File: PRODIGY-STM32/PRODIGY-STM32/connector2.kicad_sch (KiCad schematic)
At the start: 1 part, among them J2 DF40C-100DS-0.4V(51)

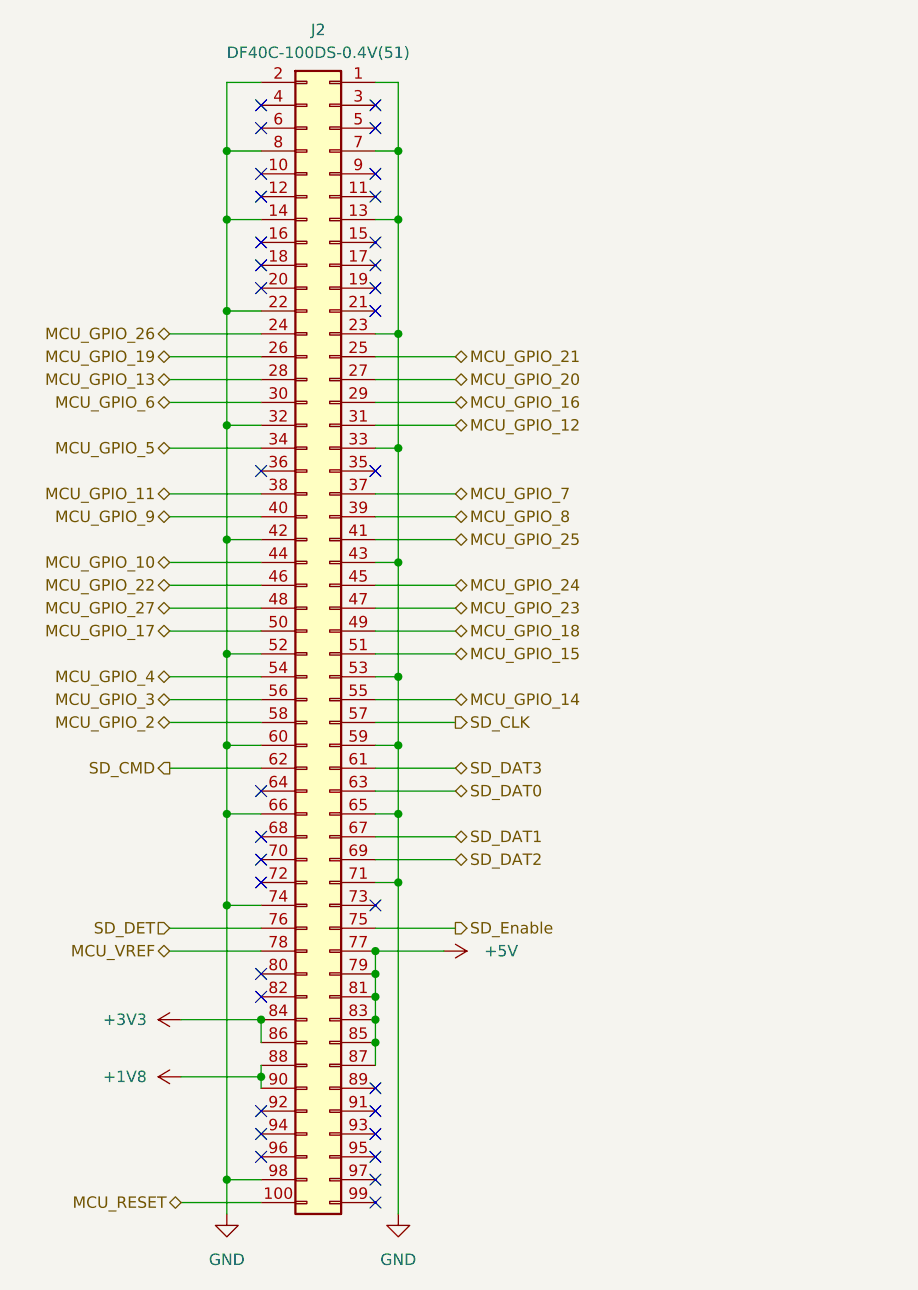
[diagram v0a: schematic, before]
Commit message: stm32 schematic finished
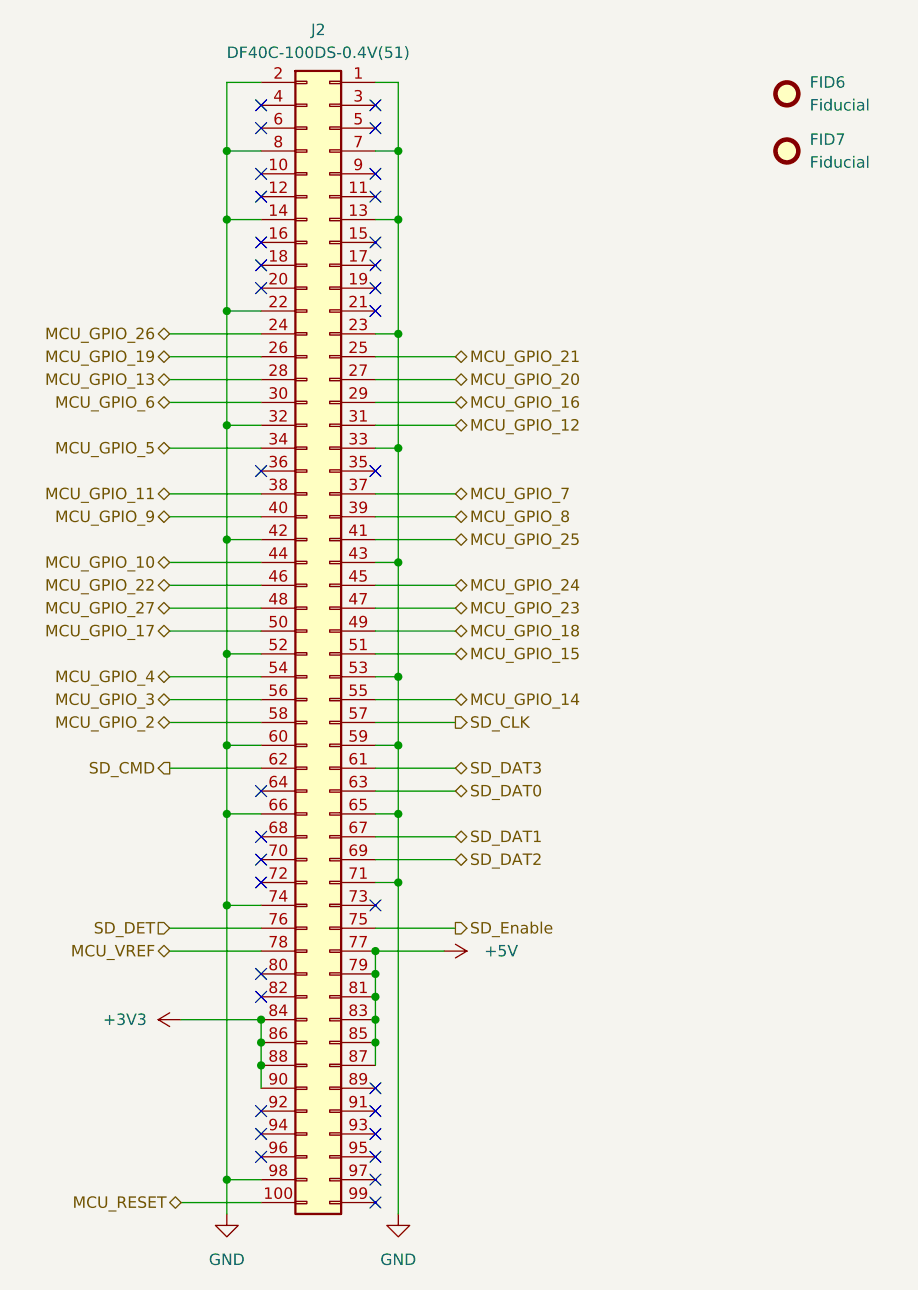
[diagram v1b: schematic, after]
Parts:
- added FID6, FID7: Fiducial, symbol Mechanical:Fiducial
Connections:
- net +1V8 is gone; now on net +3V3: J2.88, J2.90
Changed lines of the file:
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@@
+	)
+	(junction
+		(at 132.08 146.05)
+		(diameter 0)
+		(color 0 0 0 0)
 	)
 	(junction
@@
 	)
 	(junction
+		(at 132.08 143.51)
+		(diameter 0)
+		(color 0 0 0 0)
+	)
+	(junction
 		(at 144.78 143.51)
 		(diameter 0)
@@
 	)
 	(junction
-		(at 132.08 147.32)
-		(diameter 0)
-		(color 0 0 0 0)
-	)
-	(junction
 		(at 128.27 62.23)
 		(diameter 0)
@@
 	(wire
 		(pts
-			(xy 132.08 147.32) (xy 132.08 148.59)
-		)
-		(stroke
-			(width 0)
-			(type default)
-		)
-	)
-	(wire
-		(pts
 			(xy 128.27 44.45) (xy 128.27 52.07)
 		)
@@
 	(wire
 		(pts
-			(xy 132.08 147.32) (xy 132.08 146.05)
-		)
-		(stroke
-			(width 0)
-			(type default)
-		)
-	)
-	(wire
-		(pts
 			(xy 144.78 120.65) (xy 153.67 120.65)
 		)
@@
 	(wire
 		(pts
+			(xy 132.08 143.51) (xy 132.08 146.05)
+		)
+		(stroke
+			(width 0)
+			(type default)
+		)
+	)
+	(wire
+		(pts
 			(xy 147.32 52.07) (xy 147.32 44.45)
 		)
@@
 	(wire
 		(pts
-			(xy 123.19 147.32) (xy 132.08 147.32)
-		)
-		(stroke
-			(width 0)
-			(type default)
-		)
-	)
-	(wire
-		(pts
 			(xy 121.92 95.25) (xy 132.08 95.25)
 		)
@@
 		(pts
 			(xy 121.92 133.35) (xy 132.08 133.35)
+		)
+		(stroke
+			(width 0)
+			(type default)
+		)
+	)
+	(wire
+		(pts
+			(xy 132.08 146.05) (xy 132.08 148.59)
 		)
 		(stroke
@@
 		(on_board yes)
 		(dnp no)
-		(property "Reference" "#PWR023"
+		(property "Reference" "#PWR039"
 			(at 148.59 133.35 0)
 			(effects
@@
 			(project "PRODIGY-STM32"
 				(path "/f2f1c781-b8fe-416b-b7a0-b424640c1d9f/f8ef92a9-2b6b-4a6a-82b5-94550f671624"
-					(reference "#PWR023")
+					(reference "#PWR039")
 					(unit 1)
 				)
@@
 	)
 	(symbol
-		(lib_id "power:+1V8")
-		(at 123.19 147.32 90)
+		(lib_id "Mechanical:Fiducial")
+		(at 190.5 38.1 0)
 		(unit 1)
 		(exclude_from_sim no)
@@
 		(dnp no)
 		(fields_autoplaced yes)
-		(property "Reference" "#PWR020"
-			(at 127 147.32 0)
-			(effects
-				(font
-					(size 1.27 1.27)
-				)
-				(hide yes)
-			)
-		)
-		(property "Value" "+1V8"
-			(at 119.38 147.3199 90)
+		(property "Reference" "FID6"
+			(at 193.04 36.8299 0)
 			(effects
 				(font
@@
 			)
 		)
+		(property "Value" "Fiducial"
+			(at 193.04 39.3699 0)
+			(effects
+				(font
+					(size 1.27 1.27)
+				)
+				(justify left)
+			)
+		)
 		(property "Footprint" ""
-			(at 123.19 147.32 0)
-			(effects
-				(font
-					(size 1.27 1.27)
-				)
-				(hide yes)
-			)
-		)
-		(property "Datasheet" ""
-			(at 123.19 147.32 0)
-			(effects
-				(font
-					(size 1.27 1.27)
-				)
-				(hide yes)
-			)
-		)
-		(property "Description" "Power symbol creates a global label with name \"+1V8\""
-			(at 123.19 147.32 0)
-			(effects
-				(font
-					(size 1.27 1.27)
-				)
-				(hide yes)
-			)
-		)
-		(pin "1"
+			(at 190.5 38.1 0)
+			(effects
+				(font
+					(size 1.27 1.27)
+				)
+				(hide yes)
+			)
+		)
+		(property "Datasheet" "~"
+			(at 190.5 38.1 0)
+			(effects
+				(font
+					(size 1.27 1.27)
+				)
+				(hide yes)
+			)
+		)
+		(property "Description" "Fiducial Marker"
+			(at 190.5 38.1 0)
+			(effects
+				(font
+					(size 1.27 1.27)
+				)
+				(hide yes)
+			)
 		)
 		(instances
 			(project "PRODIGY-STM32"
 				(path "/f2f1c781-b8fe-416b-b7a0-b424640c1d9f/f8ef92a9-2b6b-4a6a-82b5-94550f671624"
-					(reference "#PWR020")
+					(reference "FID6")
+					(unit 1)
+				)
+			)
+		)
+	)
+	(symbol
+		(lib_id "Mechanical:Fiducial")
+		(at 190.5 44.45 0)
+		(unit 1)
+		(exclude_from_sim no)
+		(in_bom yes)
+		(on_board yes)
+		(dnp no)
+		(fields_autoplaced yes)
+		(property "Reference" "FID7"
+			(at 193.04 43.1799 0)
+			(effects
+				(font
+					(size 1.27 1.27)
+				)
+				(justify left)
+			)
+		)
+		(property "Value" "Fiducial"
+			(at 193.04 45.7199 0)
+			(effects
+				(font
+					(size 1.27 1.27)
+				)
+				(justify left)
+			)
+		)
+		(property "Footprint" ""
+			(at 190.5 44.45 0)
+			(effects
+				(font
+					(size 1.27 1.27)
+				)
+				(hide yes)
+			)
+		)
+		(property "Datasheet" "~"
+			(at 190.5 44.45 0)
+			(effects
+				(font
+					(size 1.27 1.27)
+				)
+				(hide yes)
+			)
+		)
+		(property "Description" "Fiducial Marker"
+			(at 190.5 44.45 0)
+			(effects
+				(font
+					(size 1.27 1.27)
+				)
+				(hide yes)
+			)
+		)
+		(instances
+			(project "PRODIGY-STM32"
+				(path "/f2f1c781-b8fe-416b-b7a0-b424640c1d9f/f8ef92a9-2b6b-4a6a-82b5-94550f671624"
+					(reference "FID7")
 					(unit 1)
 				)
@@
 		(dnp no)
 		(fields_autoplaced yes)
-		(property "Reference" "#PWR021"
+		(property "Reference" "#PWR037"
 			(at 128.27 168.91 0)
 			(effects
@@
 			(project "PRODIGY-STM32"
 				(path "/f2f1c781-b8fe-416b-b7a0-b424640c1d9f/f8ef92a9-2b6b-4a6a-82b5-94550f671624"
-					(reference "#PWR021")
+					(reference "#PWR037")
 					(unit 1)
 				)
@@
 		(dnp no)
 		(fields_autoplaced yes)
-		(property "Reference" "#PWR019"
+		(property "Reference" "#PWR035"
 			(at 127 140.97 0)
 			(effects
@@
 			(project "PRODIGY-STM32"
 				(path "/f2f1c781-b8fe-416b-b7a0-b424640c1d9f/f8ef92a9-2b6b-4a6a-82b5-94550f671624"
-					(reference "#PWR019")
+					(reference "#PWR035")
 					(unit 1)
 				)
@@
 		(dnp no)
 		(fields_autoplaced yes)
-		(property "Reference" "#PWR022"
+		(property "Reference" "#PWR038"
 			(at 147.32 168.91 0)
 			(effects
@@
 			(project "PRODIGY-STM32"
 				(path "/f2f1c781-b8fe-416b-b7a0-b424640c1d9f/f8ef92a9-2b6b-4a6a-82b5-94550f671624"
-					(reference "#PWR022")
+					(reference "#PWR038")
 					(unit 1)
 				)

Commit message: All footprint assosiations have been made across all schematics.
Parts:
- removed FID6, FID7: Fiducial, symbol Mechanical:Fiducial
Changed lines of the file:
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@@
-	)
-	(symbol
-		(lib_id "Mechanical:Fiducial")
-		(at 190.5 38.1 0)
-		(unit 1)
-		(exclude_from_sim no)
-		(in_bom yes)
-		(on_board yes)
-		(dnp no)
-		(fields_autoplaced yes)
-		(property "Reference" "FID6"
-			(at 193.04 36.8299 0)
-			(effects
-				(font
-					(size 1.27 1.27)
-				)
-				(justify left)
-			)
-		)
-		(property "Value" "Fiducial"
-			(at 193.04 39.3699 0)
-			(effects
-				(font
-					(size 1.27 1.27)
-				)
-				(justify left)
-			)
-		)
-		(property "Footprint" ""
-			(at 190.5 38.1 0)
-			(effects
-				(font
-					(size 1.27 1.27)
-				)
-				(hide yes)
-			)
-		)
-		(property "Datasheet" "~"
-			(at 190.5 38.1 0)
-			(effects
-				(font
-					(size 1.27 1.27)
-				)
-				(hide yes)
-			)
-		)
-		(property "Description" "Fiducial Marker"
-			(at 190.5 38.1 0)
-			(effects
-				(font
-					(size 1.27 1.27)
-				)
-				(hide yes)
-			)
-		)
-		(instances
-			(project "PRODIGY-STM32"
-				(path "/f2f1c781-b8fe-416b-b7a0-b424640c1d9f/f8ef92a9-2b6b-4a6a-82b5-94550f671624"
-					(reference "FID6")
-					(unit 1)
-				)
-			)
-		)
-	)
-	(symbol
-		(lib_id "Mechanical:Fiducial")
-		(at 190.5 44.45 0)
-		(unit 1)
-		(exclude_from_sim no)
-		(in_bom yes)
-		(on_board yes)
-		(dnp no)
-		(fields_autoplaced yes)
-		(property "Reference" "FID7"
-			(at 193.04 43.1799 0)
-			(effects
-				(font
-					(size 1.27 1.27)
-				)
-				(justify left)
-			)
-		)
-		(property "Value" "Fiducial"
-			(at 193.04 45.7199 0)
-			(effects
-				(font
-					(size 1.27 1.27)
-				)
-				(justify left)
-			)
-		)
-		(property "Footprint" ""
-			(at 190.5 44.45 0)
-			(effects
-				(font
-					(size 1.27 1.27)
-				)
-				(hide yes)
-			)
-		)
-		(property "Datasheet" "~"
-			(at 190.5 44.45 0)
-			(effects
-				(font
-					(size 1.27 1.27)
-				)
-				(hide yes)
-			)
-		)
-		(property "Description" "Fiducial Marker"
-			(at 190.5 44.45 0)
-			(effects
-				(font
-					(size 1.27 1.27)
-				)
-				(hide yes)
-			)
-		)
-		(instances
-			(project "PRODIGY-STM32"
-				(path "/f2f1c781-b8fe-416b-b7a0-b424640c1d9f/f8ef92a9-2b6b-4a6a-82b5-94550f671624"
-					(reference "FID7")
-					(unit 1)
-				)
-			)
-		)
 	)
 	(symbol

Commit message: STM32 bom done.
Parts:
- J2: value DF40C-100DS-0.4V(51) -> DF40C-100DP-04V-51; TME (none) -> DF40C-100DP-04V-51
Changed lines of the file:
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@@
 			)
 		)
-		(property "Value" "DF40C-100DS-0.4V(51)"
+		(property "Value" "DF40C-100DP-04V-51"
 			(at 138.43 33.528 0)
 			(effects
@@
 			(effects
 				(font
+					(size 1.27 1.27)
+				)
+				(hide yes)
+			)
+		)
+		(property "MOUSER" ""
+			(at 138.43 33.02 0)
+			(effects
+				(font
+					(size 1.27 1.27)
+				)
+				(hide yes)
+			)
+		)
+		(property "TME" "DF40C-100DP-04V-51"
+			(at 138.43 33.02 0)
+			(effects
+				(font

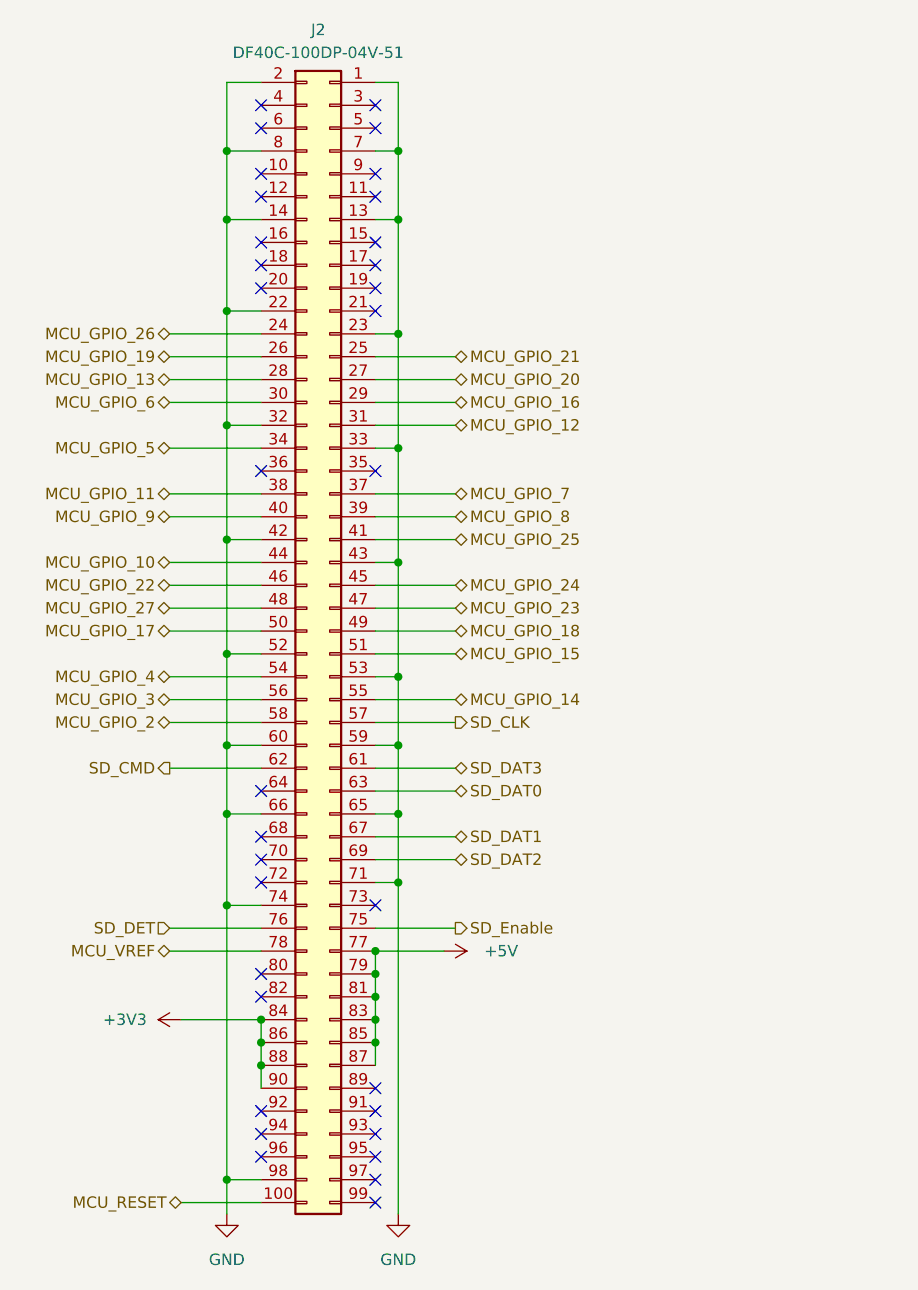
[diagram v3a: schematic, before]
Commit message: stm32 started, footprints updated, lazout started
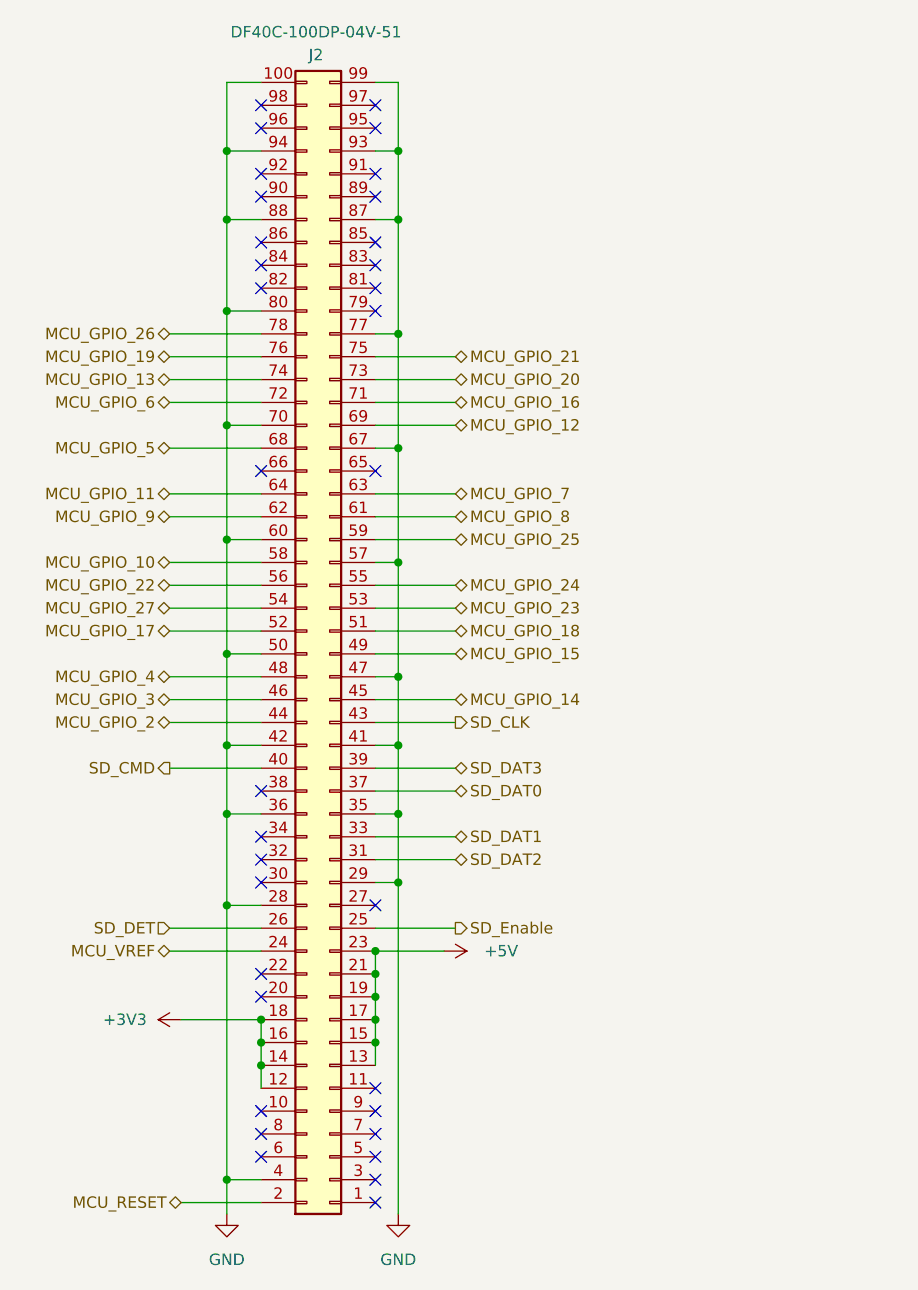
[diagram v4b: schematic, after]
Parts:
- J2: footprint DF40C:HIROSE_DF40C-100DS-0.4V_51_ -> DF40C-100DP-0:DF40C100DP04V51
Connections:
- net +3V3: now also J2.12, J2.14, J2.16, J2.18; no longer J2.84, J2.86, J2.88, J2.90
- net +5V: now also J2.13, J2.15, J2.17, J2.19, J2.21, J2.23; no longer J2.77, J2.79, J2.81, J2.83, J2.85, J2.87
- net GND: now also J2.100, J2.28, J2.29, J2.35, J2.36, J2.4, J2.41, J2.47, J2.50, J2.57, J2.67, J2.70, J2.77, J2.80, J2.87, J2.88, J2.93, J2.94, J2.99; no longer J2.1, J2.13, J2.14, J2.2, J2.22, J2.23, J2.32, J2.33, J2.43, J2.52, J2.53, J2.59, J2.65, J2.66, J2.7, J2.71, J2.74, J2.8, J2.98
- net MCU_GPIO_10: now also J2.58; no longer J2.44
- net MCU_GPIO_11: now also J2.64; no longer J2.38
- net MCU_GPIO_12: now also J2.69; no longer J2.31
- net MCU_GPIO_13: now also J2.74; no longer J2.28
- net MCU_GPIO_14: now also J2.45; no longer J2.55
- net MCU_GPIO_15: now also J2.49; no longer J2.51
- net MCU_GPIO_16: now also J2.71; no longer J2.29
- net MCU_GPIO_17: now also J2.52; no longer J2.50
- net MCU_GPIO_18: now also J2.51; no longer J2.49
- net MCU_GPIO_19: now also J2.76; no longer J2.26
- net MCU_GPIO_2: now also J2.44; no longer J2.58
- net MCU_GPIO_20: now also J2.73; no longer J2.27
- net MCU_GPIO_21: now also J2.75; no longer J2.25
- net MCU_GPIO_22: now also J2.56; no longer J2.46
- net MCU_GPIO_23: now also J2.53; no longer J2.47
- net MCU_GPIO_24: now also J2.55; no longer J2.45
- net MCU_GPIO_25: now also J2.59; no longer J2.41
- net MCU_GPIO_26: now also J2.78; no longer J2.24
- net MCU_GPIO_27: now also J2.54; no longer J2.48
- net MCU_GPIO_3: now also J2.46; no longer J2.56
- net MCU_GPIO_4: now also J2.48; no longer J2.54
- net MCU_GPIO_5: now also J2.68; no longer J2.34
- net MCU_GPIO_6: now also J2.72; no longer J2.30
- net MCU_GPIO_7: now also J2.63; no longer J2.37
- net MCU_GPIO_8: now also J2.61; no longer J2.39
- net MCU_GPIO_9: now also J2.62; no longer J2.40
- net MCU_RESET: now also J2.2; no longer J2.100
- net MCU_VREF: now also J2.24; no longer J2.78
- net SD_CLK: now also J2.43; no longer J2.57
- net SD_CMD: now also J2.40; no longer J2.62
- net SD_DAT0: now also J2.37; no longer J2.63
- net SD_DAT1: now also J2.33; no longer J2.67
- net SD_DAT2: now also J2.31; no longer J2.69
- net SD_DAT3: now also J2.39; no longer J2.61
- net SD_DET: now also J2.26; no longer J2.76
- net SD_Enable: now also J2.25; no longer J2.75
